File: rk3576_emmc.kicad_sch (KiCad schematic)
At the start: 1 part, among them U27 RK3576

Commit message: Add files via upload
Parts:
- renumbered U27 to U2
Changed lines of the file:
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@@
 		(dnp no)
 		(fields_autoplaced yes)
-		(property "Reference" "U27"
+		(property "Reference" "U2"
 			(at 102.87 35.56 0)
 			(show_name no)
@@
 			)
 		)
+		(property "Dielectric" ""
+			(at 95.25 68.58 0)
+			(hide yes)
+			(show_name no)
+			(do_not_autoplace no)
+			(effects
+				(font
+					(size 1.27 1.27)
+				)
+			)
+		)
+		(property "Voltage" ""
+			(at 95.25 68.58 0)
+			(hide yes)
+			(show_name no)
+			(do_not_autoplace no)
+			(effects
+				(font
+					(size 1.27 1.27)
+				)
+			)
+		)
+		(property "KLC_S3.3" ""
+			(at 95.25 68.58 0)
+			(hide yes)
+			(show_name no)
+			(do_not_autoplace no)
+			(effects
+				(font
+					(size 1.27 1.27)
+				)
+			)
+		)
+		(property "KLC_S4.1" ""
+			(at 95.25 68.58 0)
+			(hide yes)
+			(show_name no)
+			(do_not_autoplace no)
+			(effects
+				(font
+					(size 1.27 1.27)
+				)
+			)
+		)
+		(property "KLC_S5.1" ""
+			(at 95.25 68.58 0)
+			(hide yes)
+			(show_name no)
+			(do_not_autoplace no)
+			(effects
+				(font
+					(size 1.27 1.27)
+				)
+			)
+		)
 		(pin "1A5"
 		)
@@
 			(project "RK3576 SBC"
 				(path "/b79dbff4-0cad-4ff7-bec2-7c0e4f8b14d3/34f9b0cb-aeae-42b4-a2af-a0a79afcf392/508e51b0-6de7-4e96-b14d-74d979d6204b"
-					(reference "U27")
+					(reference "U2")
 					(unit 15)
 				)

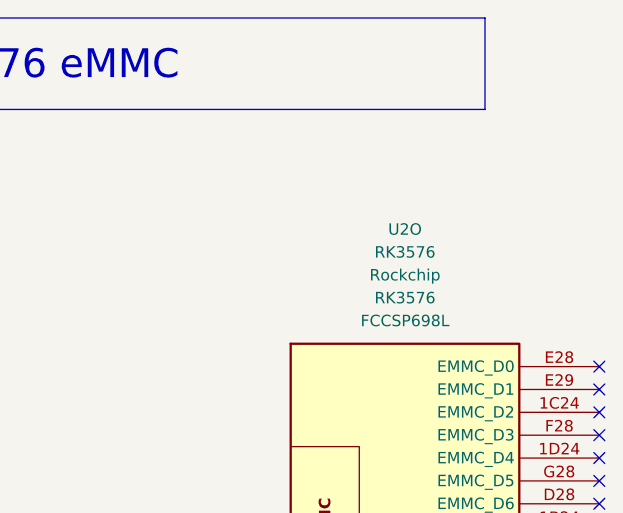
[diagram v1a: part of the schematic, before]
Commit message: SBC Board V0.2
The SBC schematics before footprint and part number check
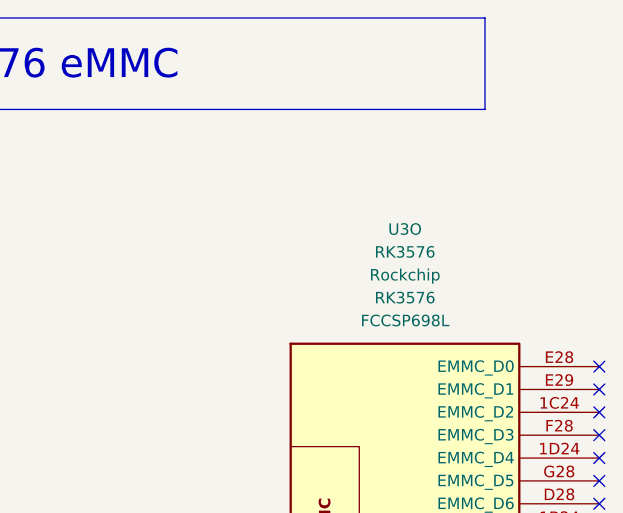
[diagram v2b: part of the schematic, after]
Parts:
- U3: renamed from U2; footprint (none) -> easyeda2kicad:FCCSP-698_L17.2-W16.1-TL_RK3576
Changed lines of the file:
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@@
 		(dnp no)
 		(fields_autoplaced yes)
-		(property "Reference" "U2"
+		(property "Reference" "U3"
 			(at 102.87 35.56 0)
 			(show_name no)
@@
 			)
 		)
-		(property "Footprint" ""
+		(property "Footprint" "easyeda2kicad:FCCSP-698_L17.2-W16.1-TL_RK3576"
 			(at 27.94 5.715 0)
 			(hide yes)
@@
 			(project "RK3576 SBC"
 				(path "/b79dbff4-0cad-4ff7-bec2-7c0e4f8b14d3/34f9b0cb-aeae-42b4-a2af-a0a79afcf392/508e51b0-6de7-4e96-b14d-74d979d6204b"
-					(reference "U2")
+					(reference "U3")
 					(unit 15)
 				)

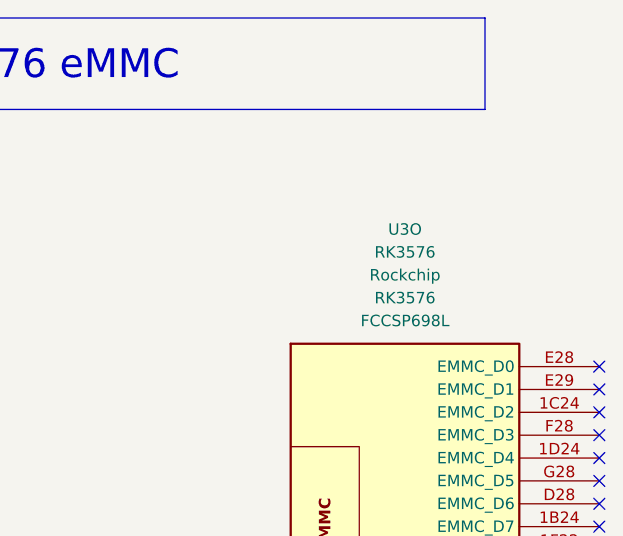
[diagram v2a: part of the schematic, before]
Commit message: SBCv0.3
there is no big thing update just some LCSC & Mouser parts
and Big problem deleted alot of component values (:
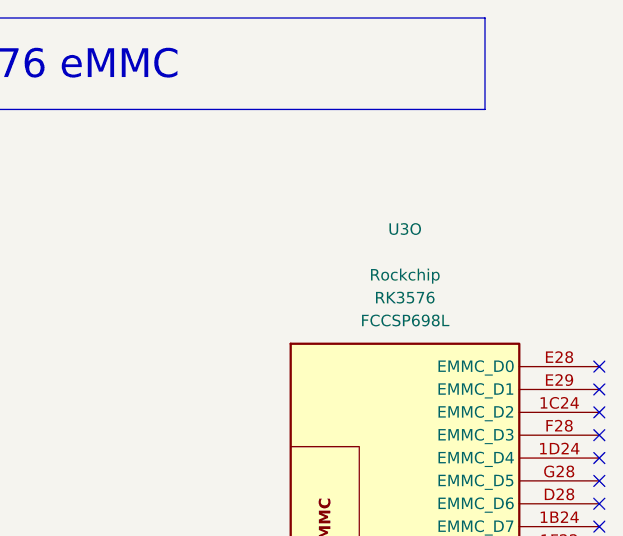
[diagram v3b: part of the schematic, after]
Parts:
- U3: value RK3576 -> (none); LCSC Part (none) -> (polyline
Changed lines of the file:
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@@
 			)
 		)
-		(property "Value" "RK3576"
+		(property "Value" ""
 			(at 102.87 38.1 0)
 			(show_name no)
@@
 			)
 		)
-		(property "KLC_S5.1" ""
+		(property "LCSC Part" "(polyline"
 			(at 95.25 68.58 0)
 			(hide yes)
@@
 			)
 		)
+		(property "KLC_S4.2_DVDD" ""
+			(at 95.25 68.58 0)
+			(hide yes)
+			(show_name no)
+			(do_not_autoplace no)
+			(effects
+				(font
+					(size 1.27 1.27)
+				)
+			)
+		)
+		(property "KLC_S4.2_VREG_LX" ""
+			(at 95.25 68.58 0)
+			(hide yes)
+			(show_name no)
+			(do_not_autoplace no)
+			(effects
+				(font
+					(size 1.27 1.27)
+				)
+			)
+		)
 		(pin "1A5"
 		)
@@
 					(reference "U3")
 					(unit 15)
+					(variant
+						(name "Test")
+					)
 				)
 			)

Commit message: SBCv0.4
add LCSC & Mouser parts 
and solve the deleted value in the past version
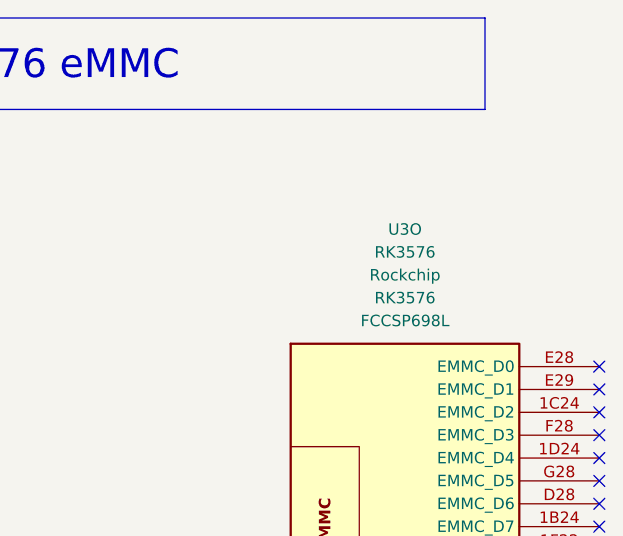
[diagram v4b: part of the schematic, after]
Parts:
- U3: value (none) -> RK3576; LCSC Part (polyline -> C42388007
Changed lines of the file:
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@@
 			)
 		)
-		(property "Value" ""
+		(property "Value" "RK3576"
 			(at 102.87 38.1 0)
 			(show_name no)
@@
 			)
 		)
-		(property "LCSC Part" "(polyline"
+		(property "LCSC Part" "C42388007"
 			(at 95.25 68.58 0)
 			(hide yes)
